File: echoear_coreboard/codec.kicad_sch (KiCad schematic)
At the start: 0 parts

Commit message: Starting codec SCH
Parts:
- added C12, C13: 1u, Capacitor_SMD:C_0402_1005Metric, symbol Device:C
- added Q3, Q4: LBSS138DW1T1G, easyeda2kicad:SC-88-6_L2.0-W1.3-P0.65-LS2.1-BL, symbol Sym_easyeda2kicad:LBSS138DW1T1G
- added R15, R6: 2.2k, Resistor_SMD:R_0402_1005Metric, symbol Device:R
- added R7: R, symbol Device:R
- added U4: XC6206P332MR, easyeda2kicad:SOT-23-3_L2.9-W1.6-P1.90-LS2.8-BR, symbol Sym_easyeda2kicad:XC6206P332MR
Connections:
- new net: C13.2, U4.1 (GND)
- new net AUDIO_I2C_SCL: Q4.4 (S), R15.2
- new net AUDIO_I2C_SDA: Q3.4 (S), R6.2
- new net CODEC_3V3: C13.1, Q3.5 (G), Q4.5 (G), R15.1, R6.1, U4.2 (Vout)
- new net ES_I2C_SCL: Q4.3 (D)
- new net ES_I2C_SDA: Q3.3 (D)
- new net MCU_3V3: U4.3 (Vin)
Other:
- note added: "CODEC 3V3 LDO"
- note added: "CODEC_IIC"

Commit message: Codec SCH until ES8311, ERC non verified
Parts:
- added C10: 2.2n, Capacitor_SMD:C_0402_1005Metric, symbol Device:C
- added C11: 100p, Capacitor_SMD:C_0402_1005Metric, symbol Device:C
- added C14, C7: 470n, Capacitor_SMD:C_0402_1005Metric, symbol Device:C
- added C15, C8: 220n, Capacitor_SMD:C_0402_1005Metric, symbol Device:C
- added C9: 10n, Capacitor_SMD:C_0402_1005Metric, symbol Device:C
- added R10: 4.3k, Capacitor_SMD:C_0402_1005Metric, symbol Device:R
- added R11, R7: 2.2k, Resistor_SMD:R_0402_1005Metric, symbol Device:R
- added R12, R8: 10k, Resistor_SMD:R_0402_1005Metric, symbol Device:R
- added R13: 20k, Capacitor_SMD:C_0402_1005Metric, symbol Device:R
- added R9: 20k, Resistor_SMD:R_0402_1005Metric, symbol Device:R
- R14: renamed from R7; value R -> 0R; footprint (none) -> Resistor_SMD:R_0402_1005Metric; LCSC (none) -> C17168
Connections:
- net MCU_3V3: now also C12.1
- net GNDA: now reaches C13.2, U4.1 (GND)
- net GNDA: now also R14.1
- net GND: now reaches R14.2
- net GND: now also C12.2
- new net: C10.2, R12.1, R13.2
- new net: C14.1, R12.2
- new net: C11.2, C15.2, R10.1, R13.1
- new net: C11.1, C8.2, R10.2, R9.1
- new net: C7.2, R8.1
- new net: C10.1, R8.2, R9.2
- new net: C14.2, C9.2, R11.2
- new net: C7.1, C9.1, R7.2
- new net ADC_MIC3_N: C15.1
- new net ADC_MIC3_P: C8.1
- new net OUTN: R11.1
- new net OUTP: R7.1
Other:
- note added: "AEC"
- note added: "ES8311"
- moved on the sheet: C12, C13, R14, U4

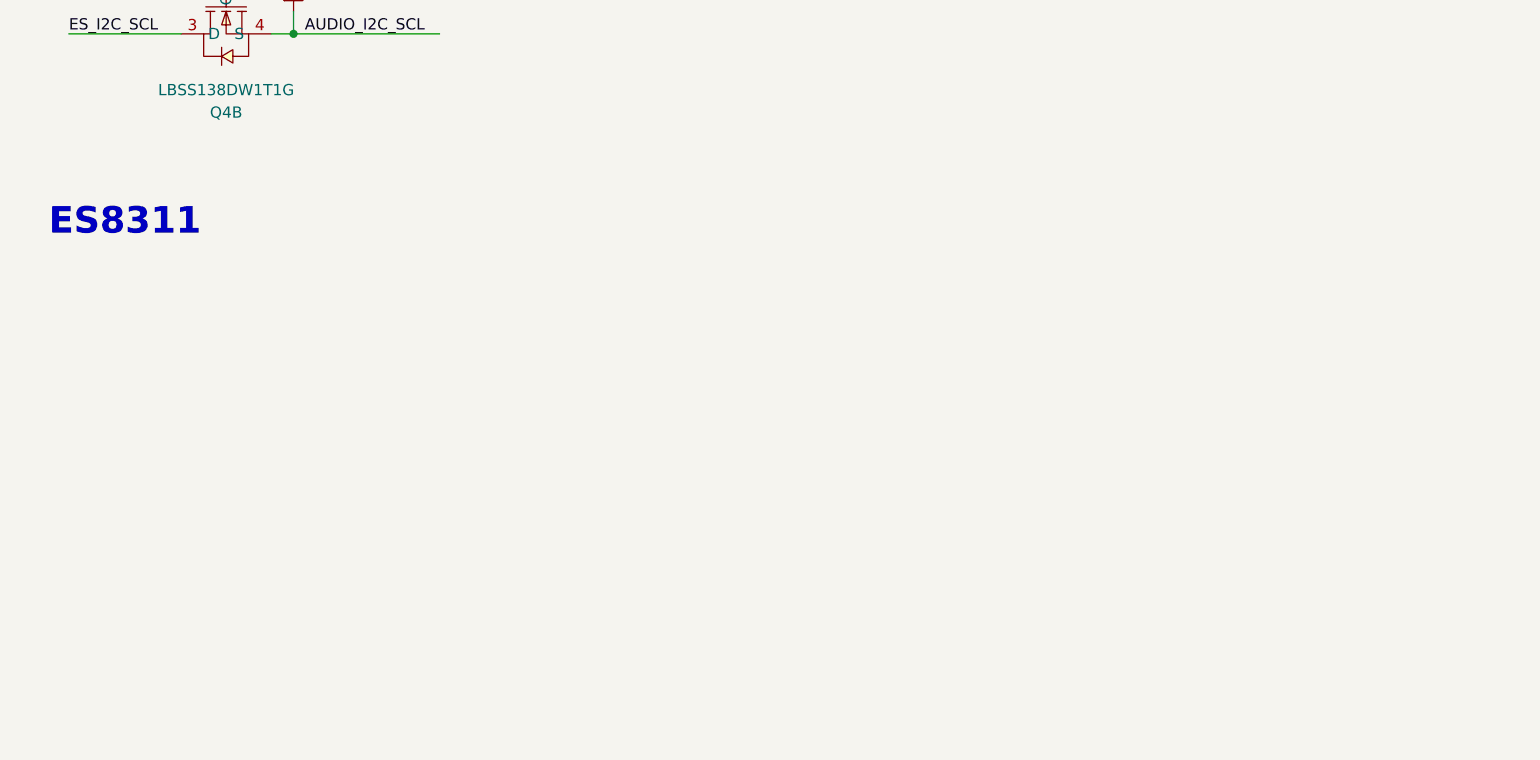
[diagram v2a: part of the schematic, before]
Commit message: Half of ES8311 SCH done
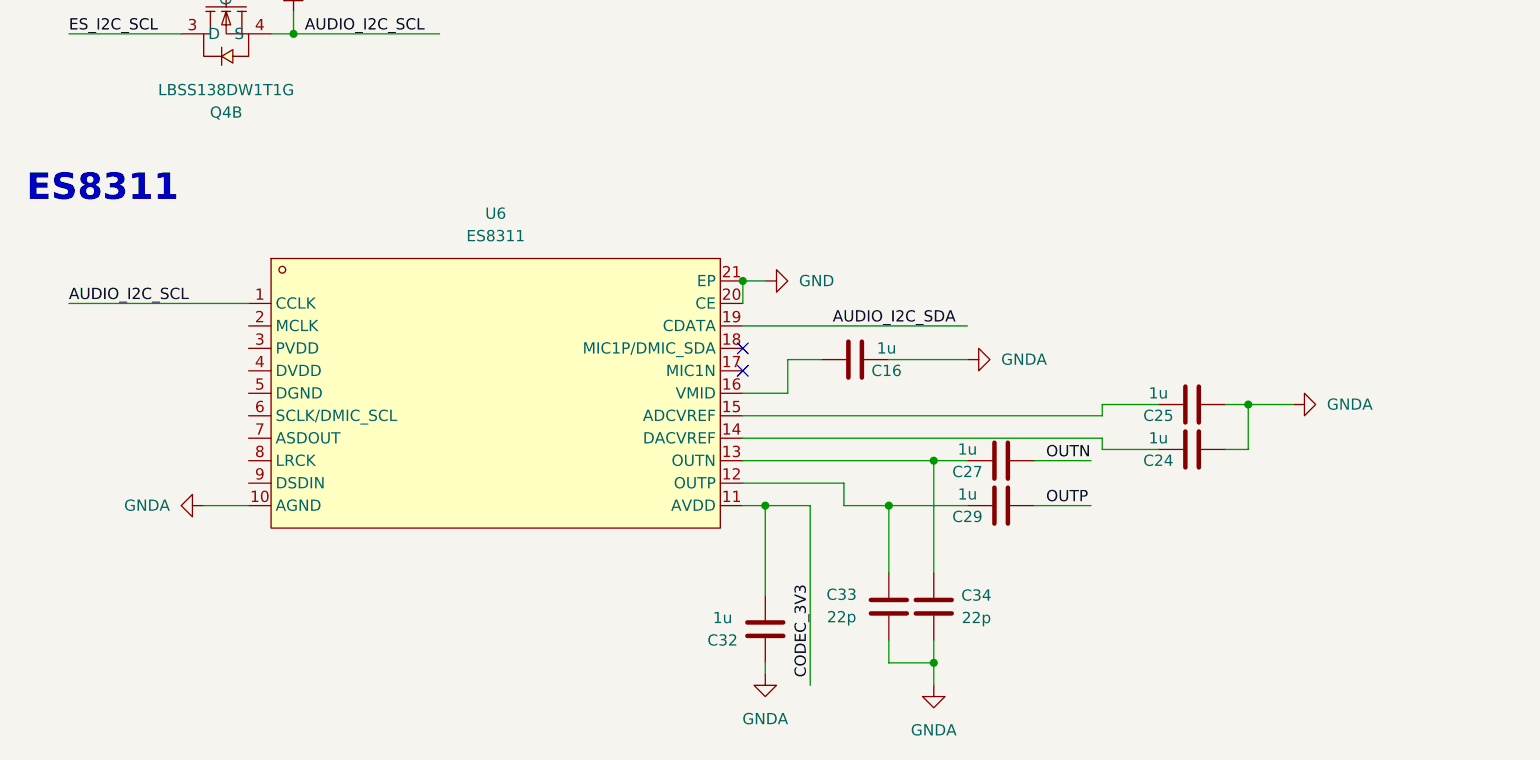
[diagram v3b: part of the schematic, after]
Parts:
- added C16, C24, C25, C27, C29, C32: 1u, Capacitor_SMD:C_0402_1005Metric, symbol Device:C
- added C33, C34: 22p, Capacitor_SMD:C_0402_1005Metric, symbol Device:C
- added U6: ES8311, easyeda2kicad:WQFN-20_L3.0-W3.0-P0.40-BL-EP1.7, symbol Sym_easyeda2kicad:ES8311
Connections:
- net AUDIO_I2C_SCL: now also U6.1 (CCLK)
- net AUDIO_I2C_SDA: now also U6.19 (CDATA)
- net CODEC_3V3: now also C32.2, U6.11 (AVDD)
- net GND: now also U6.20 (CE), U6.21 (EP)
- net GNDA: now also C16.2, C24.2, C25.2, C32.1, C33.1, C34.2, U6.10 (AGND)
- net OUTN: now also C27.2
- net OUTP: now also C29.2
- new net: C29.1, C33.2, U6.12 (OUTP)
- new net: C16.1, U6.16 (VMID)
- new net: C27.1, C34.1, U6.13 (OUTN)
- new net: C24.1, U6.14 (DACVREF)
- new net: C25.1, U6.15 (ADCVREF)
- no-connect marks 0 -> 2

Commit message: Stopped before ES7210
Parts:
- added C30: 1u, Capacitor_SMD:C_0402_1005Metric, symbol Device:C
- added C31: 100n, Capacitor_SMD:C_0402_1005Metric, symbol Device:C
- added C39, C40, C41: 22p, Capacitor_SMD:C_0402_1005Metric, symbol Device:C
- added U5: ES7210, easyeda2kicad:QFN-32_L4.0-W4.0-P0.40-BL-EP2.7, symbol Sym_easyeda2kicad:ES7210
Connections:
- net CODEC_3V3: now also U6.3 (PVDD), U6.4 (DVDD), C30.2, C31.2
- net GNDA: now also U6.5 (DGND), C30.1, C31.1, C39.1, C40.1, C41.1
- net I2S_MCLK: now reaches U6.2 (MCLK)
- net I2S_MCLK: now also C39.2
- net I2S_BCK: now reaches U6.6 (SCLK/DMIC_SCL)
- net I2S_BCK: now also C40.2
- net I2S_WS: now reaches U6.8 (LRCK)
- net I2S_WS: now also C41.2
- net I2S_DO: now reaches U6.9 (DSDIN)
- no-connect marks 2 -> 3
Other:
- note added: "ES7210"
